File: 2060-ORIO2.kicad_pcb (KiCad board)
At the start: 4 copper layers, 100 x 100 mm, 185 parts, among them J11 RaspberryPI-B+header, J12 Conn_01x04, J13 Conn_01x08, J14 Conn_01x02, J15 Conn_01x08, J16 Conn_01x10, J17 Conn_01x10, J18 Conn_01x10, J19 Conn_01x10, J20 Conn_01x09, J21 Conn_01x08, J22 Conn_01x08, J23 Conn_01x08, J24 Conn_01x08, J25 Conn_01x08, J26 Conn_01x08, J28 Conn_01x16, J29 Conn_01x16, J30 Conn_01x16, J31 Conn_01x08, J32 Conn_01x08, J33 Conn_01x08, J34 Conn_01x08, J35 TBL001-500-02GY-2GY, Q11 ULN2803ADWR, Q12 BCV27, Q91 BCV27, Q92 BCV27, Q93 BCV27, Q94 BCV27, SW1 SW_DIP_x01, SW11 SW_DIP_x08, U11 ICE40HX4K-TQ144, U12 ‎74LVT245B, U13 ‎74LVT245B, U14 ‎74LVT245B, U15 AP63300, U16 MCP3008, U17 AZ1117CH-3.3TRG1, U18 AZ1117CH-3.3TRG1, U19 AZ1117CH-1.2, U20 AP63300, U21 ‎74LVT245B, U22 ‎74LVT245B, U23 ‎74LVT245B, U24 ‎74LVT245B, U25 AP63300, U26 AP3012, Y11 XLH536025_000000I

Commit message: Revision 2 as ordered from JLCPCB
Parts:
- added C66: 22uF, Capacitor_SMD:C_0805_2012Metric_Pad1.15x1.40mm_HandSolder, F.Cu at (82.8, 58.4)
- added C67: 22uF, Capacitor_SMD:C_0805_2012Metric_Pad1.15x1.40mm_HandSolder, F.Cu at (82.8, 56.4)
- added C69: 22uF, Capacitor_SMD:C_0805_2012Metric_Pad1.15x1.40mm_HandSolder, F.Cu at (75.0, 121.4)
- added C71: 22uF, Capacitor_SMD:C_0805_2012Metric_Pad1.15x1.40mm_HandSolder, F.Cu at (77.0, 121.4)
- added C72: 22uF, Capacitor_SMD:C_0805_2012Metric_Pad1.15x1.40mm_HandSolder, F.Cu at (114.4, 116.9)
- added C73: 22uF, Capacitor_SMD:C_0805_2012Metric_Pad1.15x1.40mm_HandSolder, F.Cu at (112.5, 116.9)
- added J27: Conn_01x02, Connector_PinHeader_2.54mm:PinHeader_1x02_P2.54mm_Vertical, F.Cu at (83.0, 96.0)
- added Q13: BCV27, Package_TO_SOT_SMD:SOT-23, F.Cu at (90.5, 88.0)
- added R12: 1K, Resistor_SMD:R_0603_1608Metric_Pad1.05x0.95mm_HandSolder, F.Cu at (93.2, 88.0)
- Q91, Q92, Q93, Q94: value BCV27 -> BCW65ALT1G
- moved SW1 7.62 mm to (122.1, 108.4), turned to 180 degrees
- moved Q12 3.35 mm to (89.9, 99.3)
- moved R54 3.35 mm to (93.3, 100.2)
- moved J14 2.62 mm to (83.0, 98.6), turned to 90 degrees
- moved C46 1.21 mm to (76.2, 126.4)
- moved C48 1.21 mm to (74.2, 126.4)
- moved C50 0.51 mm to (87.2, 56.9)
- moved C58 0.51 mm to (87.2, 58.9)
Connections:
- SW1 pad 1: VCC_IO -> Net-(R36-Pad1)
- SW1 pad 2: Net-(R36-Pad1) -> VCC_IO
- U11 pad 26: /IOL_18B -> /FPGA_AIR
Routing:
- net /FPGA_AIR: track 0.00 -> 63.2 mm, vias 0 -> 2
- net +BATT: track 196.5 -> 227.3 mm, vias 18 -> 20
- net VCC_PWM: track 43.5 -> 71.1 mm, vias 0 -> 2
- net VCC_IO: track 284.4 -> 310.4 mm, vias 4 -> 6
- net GND: track 107.0 -> 125.4 mm, vias 127 -> 164
- net Net-(J27-Pad2): track 0.00 -> 9.70 mm
- net Net-(R36-Pad1): track 0.00 -> 9.11 mm
- net Net-(C35-Pad2): track 0.00 -> 8.00 mm
- net Net-(C60-Pad2): track 0.00 -> 7.03 mm
- net Net-(C65-Pad2): track 0.00 -> 4.68 mm
- net Net-(C49-Pad2): track 0.00 -> 4.68 mm
- net /VB_RSL: track 25.9 -> 29.7 mm
- net Net-(C60-Pad1): track 0.00 -> 1.82 mm
- net Net-(C35-Pad1): track 0.00 -> 1.73 mm
- net Net-(Q13-Pad1): track 0.00 -> 1.67 mm
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- added copper zone on F.Cu, net +BATT
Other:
- board text added: "AIR"

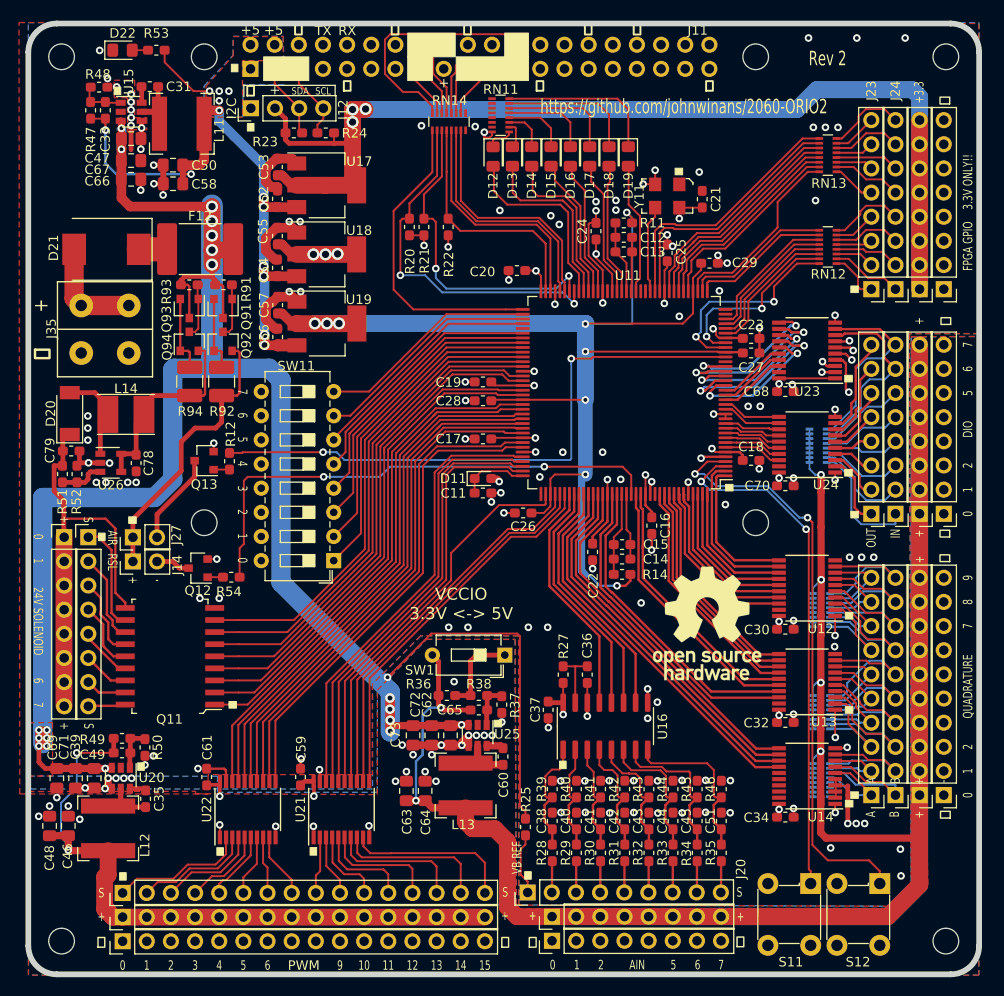
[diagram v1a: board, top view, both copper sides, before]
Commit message: Move the PI connector, add filter caps, & tweak current limiter.
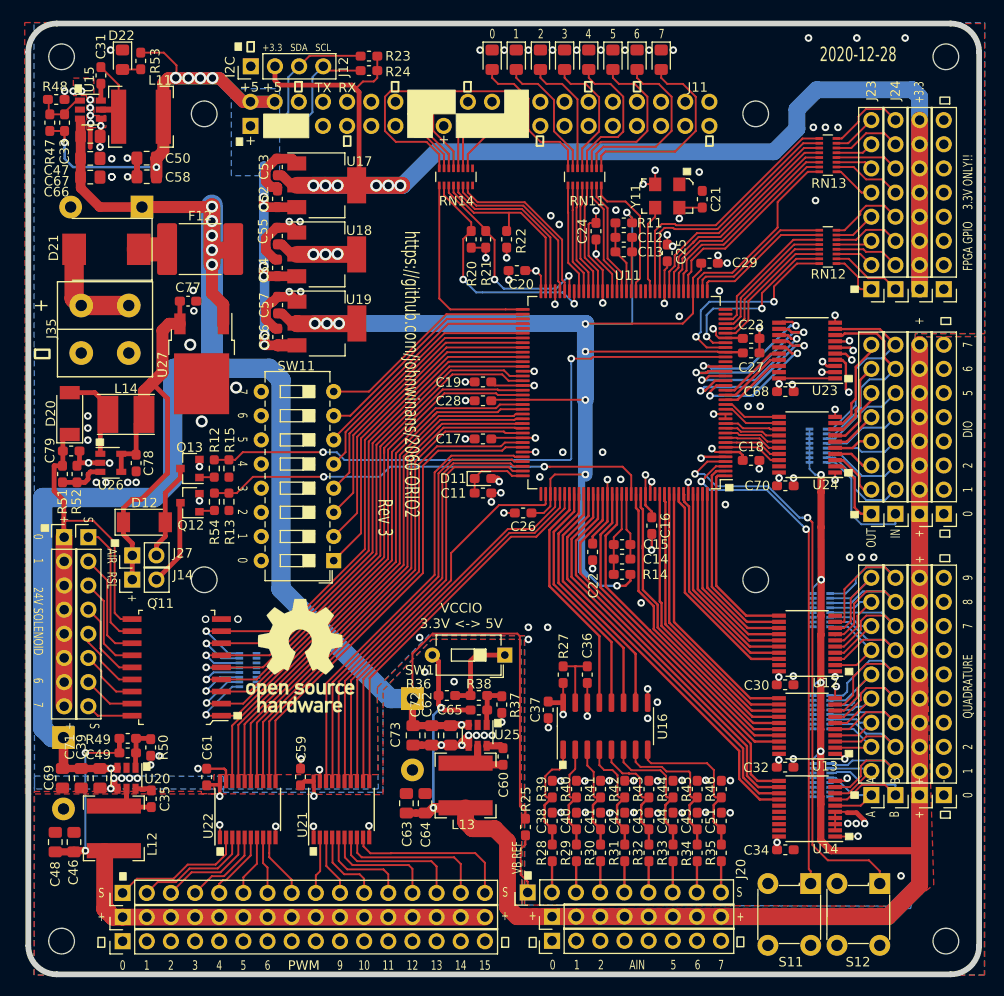
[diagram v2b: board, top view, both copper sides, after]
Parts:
- removed D13: LED_ALT, LED_SMD:LED_0805_2012Metric_Pad1.15x1.40mm_HandSolder
- removed Q91, Q92, Q93, Q94: BCW65ALT1G, Package_TO_SOT_SMD:SOT-23
- removed R91, R93: 10K, Resistor_SMD:R_0603_1608Metric_Pad1.05x0.95mm_HandSolder
- removed R92, R94: 1.2, Resistor_SMD:R_1210_3225Metric_Pad1.42x2.65mm_HandSolder
- added C74: 3300uF, Capacitor_THT:CP_Radial_D16.0mm_P7.50mm, B.Cu at (84.0, 61.3)
- added C75: 3300uF, Capacitor_THT:CP_Radial_D16.0mm_P7.50mm, B.Cu at (75.7, 117.1)
- added C76: 3300uF, Capacitor_THT:CP_Radial_D16.0mm_P7.50mm, B.Cu at (112.4, 113.0)
- added C77: .1uF, Capacitor_SMD:C_0603_1608Metric_Pad1.08x0.95mm_HandSolder, F.Cu at (88.8, 71.2)
- added D1: LED_ALT, LED_SMD:LED_0805_2012Metric_Pad1.15x1.40mm_HandSolder, F.Cu at (123.3, 45.8)
- added D12: DB2460600L, Diode_SMD:D_SOD-128, F.Cu at (84.2, 94.5)
- added R13: 1K, Resistor_SMD:R_0603_1608Metric_Pad0.98x0.95mm_HandSolder, F.Cu at (93.1, 92.3)
- added R15: 1K, Resistor_SMD:R_0603_1608Metric_Pad0.98x0.95mm_HandSolder, F.Cu at (93.1, 88.8)
- added RN15: 1K, Resistor_SMD:R_Array_Convex_8x0602, B.Cu at (95.1, 110.0)
- added U27: MC7812BDTG, Package_TO_SOT_SMD:TO-252-2, F.Cu at (90.2, 77.8)
- Q12, Q13: value BCV27 -> SSM3K376R
- R12, R54: value 1K -> 100; footprint Resistor_SMD:R_0603_1608Metric_Pad1.05x0.95mm_HandSolder -> Resistor_SMD:R_0603_1608Metric_Pad0.98x0.95mm_HandSolder
- moved LOGO11 42.9 mm to (100.6, 108.5)
- moved R23 11.3 mm to (107.8, 45.4), turned to 0 degrees
- moved RN11 11.0 mm to (130.5, 58.1), turned to 90 degrees
- moved D7 10.7 mm to (138.6, 45.8)
- moved D6 10.6 mm to (136.0, 45.8)
- moved D5 10.5 mm to (133.5, 45.8)
- moved D4 10.4 mm to (130.9, 45.8)
- moved D3 10.3 mm to (128.4, 45.8)
- moved D2 10.2 mm to (125.9, 45.8)
- moved D0 10.2 mm to (120.8, 45.8)
- moved R54 8.13 mm to (91.6, 92.3), turned to 90 degrees
- moved R24 7.98 mm to (107.8, 47.0)
- moved Q12 6.93 mm to (89.0, 92.4)
- moved R20 6.63 mm to (118.6, 64.7)
- moved R21 6.63 mm to (120.1, 64.7)
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- renumbered D12 to D0, D14 to D2, D15 to D3, D16 to D4, D17 to D5, D18 to D6, D19 to D7
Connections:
- C78 pad 1: /VB_RSOL -> /VB_LIM
- D0 pad 1: Net-(D12-Pad1) -> GND
- D0 pad 2: /LED_0 -> Net-(D0-Pad2)
- D2 pad 1: Net-(D14-Pad1) -> GND
- D2 pad 2: /LED_2 -> Net-(D2-Pad2)
- D3 pad 1: Net-(D15-Pad1) -> GND
- D3 pad 2: /LED_3 -> Net-(D3-Pad2)
- D4 pad 1: Net-(D16-Pad1) -> GND
- D4 pad 2: /LED_4 -> Net-(D4-Pad2)
- D5 pad 1: Net-(D17-Pad1) -> GND
- D5 pad 2: /LED_5 -> Net-(D5-Pad2)
- D6 pad 1: Net-(D18-Pad1) -> GND
- D6 pad 2: /LED_6 -> Net-(D6-Pad2)
- D7 pad 1: Net-(D19-Pad1) -> GND
- D7 pad 2: /LED_7 -> Net-(D7-Pad2)
- J14 pad 1: /VB_RSL -> /VB_LIM
- J27 pad 1: /VB_RSL -> /VB_LIM
- L14 pad 1: /VB_RSOL -> /VB_LIM
- RN11 pad 1: Net-(D12-Pad1) -> /LED_0
- RN11 pad 10: GND -> Net-(D6-Pad2)
- RN11 pad 11: GND -> Net-(D5-Pad2)
- RN11 pad 12: GND -> Net-(D4-Pad2)
- RN11 pad 13: GND -> Net-(D3-Pad2)
- RN11 pad 14: GND -> Net-(D2-Pad2)
- RN11 pad 15: GND -> Net-(D1-Pad2)
- RN11 pad 16: GND -> Net-(D0-Pad2)
- RN11 pad 2: Net-(D13-Pad1) -> /LED_1
- RN11 pad 3: Net-(D14-Pad1) -> /LED_2
- RN11 pad 4: Net-(D15-Pad1) -> /LED_3
- RN11 pad 5: Net-(D16-Pad1) -> /LED_4
- RN11 pad 6: Net-(D17-Pad1) -> /LED_5
- RN11 pad 7: Net-(D18-Pad1) -> /LED_6
- RN11 pad 8: Net-(D19-Pad1) -> /LED_7
- RN11 pad 9: GND -> Net-(D7-Pad2)
- U26 pad 4: /VB_RSOL -> /VB_LIM
- U26 pad 5: /VB_RSOL -> /VB_LIM
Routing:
- net /VB_LIM: track 0.00 -> 46.6 mm
- net /VB_RSL: track 29.7 -> 0.00 mm
- net /VB_RSOL: track 21.3 -> 0.00 mm
- net Net-(D7-Pad2): track 0.00 -> 21.3 mm
- net Net-(D6-Pad2): track 0.00 -> 19.4 mm
- net Net-(D5-Pad2): track 0.00 -> 17.5 mm
- net VCC_IO_3.3: track 130.5 -> 147.4 mm, vias 3 -> 6
- net Net-(D19-Pad1): track 16.9 -> 0.00 mm
- net Net-(D0-Pad2): track 0.00 -> 15.9 mm
- net Net-(D4-Pad2): track 0.00 -> 15.5 mm
- net Net-(D18-Pad1): track 14.4 -> 0.00 mm
- net Net-(D1-Pad2): track 0.00 -> 13.8 mm
- net +BATT: track 227.3 -> 213.7 mm, vias 20 -> 7
- net Net-(D3-Pad2): track 0.00 -> 13.6 mm
- net Net-(D2-Pad2): track 0.00 -> 13.0 mm
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- removed copper zone on B.Cu, net +BATT
- removed copper zone on F.Cu, net +BATT
- removed copper zone on In1.Cu, net +BATT
- removed copper zone on In2.Cu, net +BATT
- removed copper zone on F.Cu, net 5V_PI
- removed copper zone on In2.Cu, net 5V_PI
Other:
- board text added: "2020-12-28"
- board text added: "Rev 3"
- board text removed: "Rev 2"

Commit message: Change 12V LDO, header & cap clearance
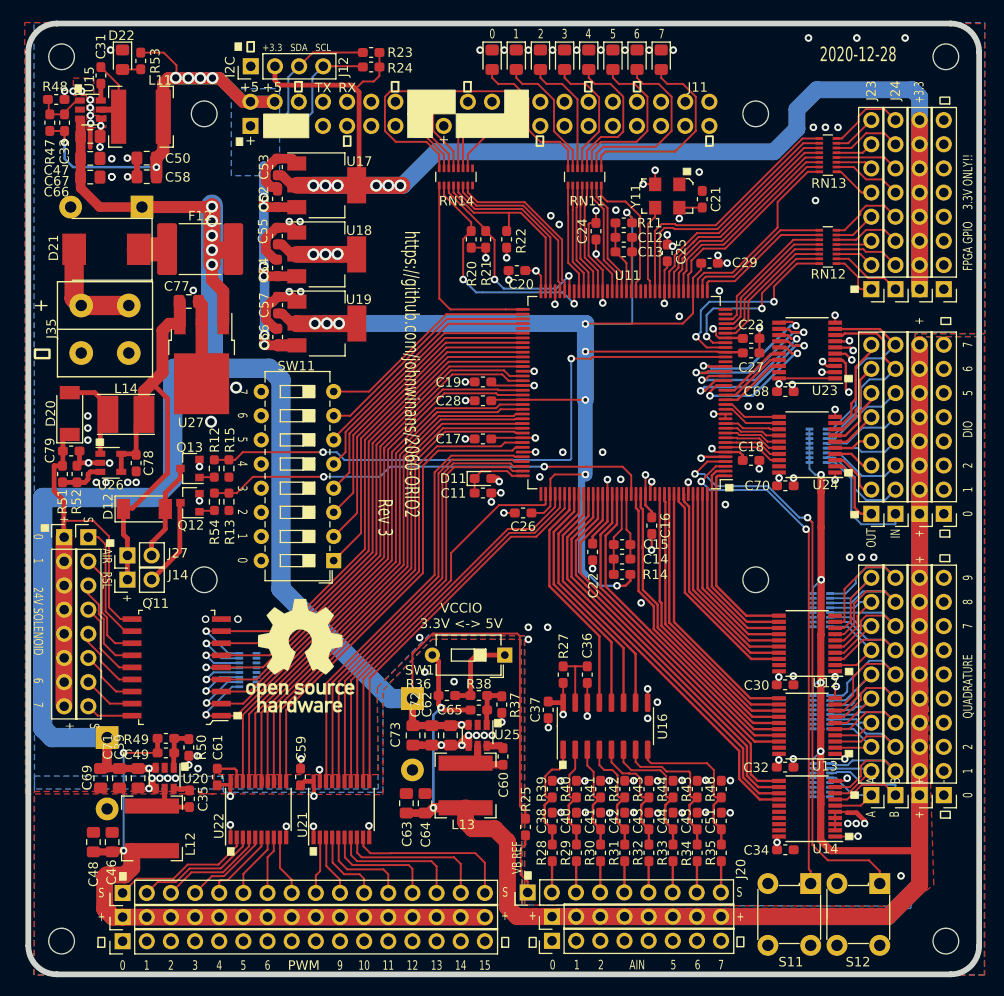
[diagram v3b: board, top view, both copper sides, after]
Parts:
- C77: value .1uF -> 22uF; footprint Capacitor_SMD:C_0603_1608Metric_Pad1.08x0.95mm_HandSolder -> Capacitor_SMD:C_0805_2012Metric_Pad1.15x1.40mm_HandSolder
- U27: value MC7812BDTG -> LM2940IMP-12/NOPB; footprint Package_TO_SOT_SMD:TO-252-2 -> Package_TO_SOT_SMD:TO-252-3_TabPin2
- moved C75 4.59 mm to (80.3, 117.1)
- moved C71 4.01 mm to (81.6, 121.4)
- moved L12 4.01 mm to (85.0, 126.6)
- moved C35 4.01 mm to (88.9, 123.5)
- moved C39 4.01 mm to (83.5, 121.4)
- moved C46 4.01 mm to (80.8, 128.1)
- moved C48 4.01 mm to (78.8, 128.1)
- moved C49 4.01 mm to (86.5, 118.7)
- moved C69 4.01 mm to (79.6, 121.4)
- moved R49 4.01 mm to (86.5, 117.2)
- moved R50 4.01 mm to (88.9, 118.1)
- moved U20 4.01 mm to (86.3, 121.4)
- moved D12 1.40 mm to (84.2, 93.1)
- moved C61 1.12 mm to (91.9, 121.2)
- moved U22 1.12 mm to (96.2, 124.7)
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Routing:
- net GND: track 118.7 -> 128.1 mm, vias 158 -> 156
- net +BATT: track 213.7 -> 218.3 mm
- net VCC_PWM: track 68.1 -> 70.4 mm
- net /PWM4: track 7.20 -> 8.11 mm
- net /PWM1: track 12.2 -> 13.1 mm
- net /FPGA_PWM6: track 52.1 -> 51.3 mm
- net /FPGA_PWM1: track 56.4 -> 55.6 mm
- net /FPGA_PWM7: track 51.3 -> 50.4 mm
- net /FPGA_PWM2: track 55.6 -> 54.8 mm
- net /SDA1: track 14.3 -> 15.1 mm
- net /FPGA_PWM0: track 57.6 -> 56.8 mm
- net /PWM0: track 14.1 -> 15.0 mm
- net /PWM2: track 10.4 -> 11.2 mm
- net /PWM3: track 8.54 -> 9.21 mm
- net /PWM5: track 6.23 -> 6.89 mm
